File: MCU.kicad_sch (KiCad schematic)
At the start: 22 parts, among them J1 USB_C_Receptacle_USB2.0_16P, SW1 SW_Push_Open, U1 STM32H743VITx, Y1 Crystal

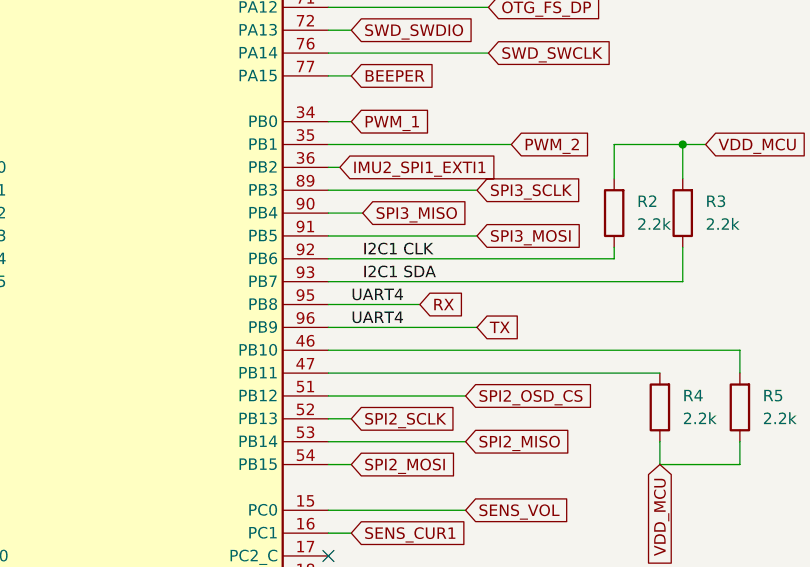
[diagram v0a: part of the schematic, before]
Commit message: finshed every schematic pages, remains footprints assignments
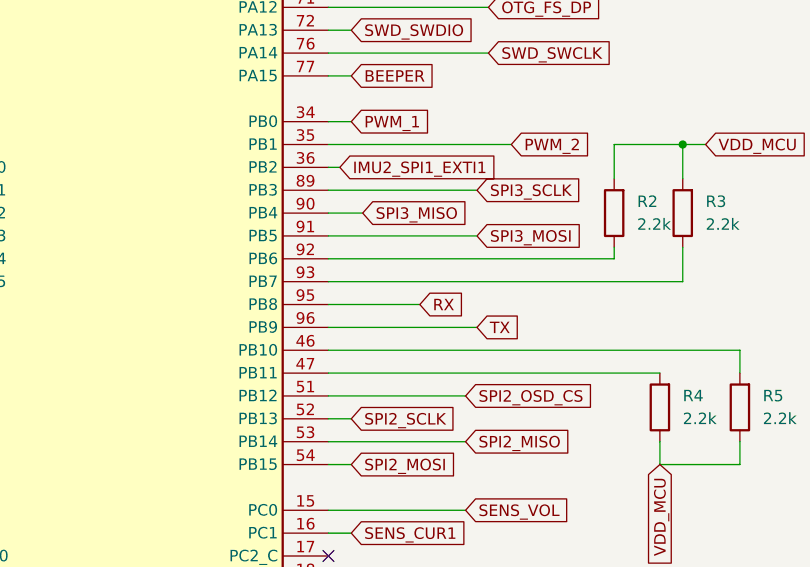
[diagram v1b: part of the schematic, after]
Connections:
- net I2C1 CLK: no longer names the net of R2.1, U1.92 (PB6)
- net I2C1 SDA: no longer names the net of R3.1, U1.93 (PB7)
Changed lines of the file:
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@@
-		)
-	)
-	(label "I2C1 CLK"
-		(at 162.56 95.25 0)
-		(effects
-			(font
-				(size 1.27 1.27)
-			)
-			(justify left bottom)
-		)
-	)
-	(label "UART4"
-		(at 161.29 102.87 0)
-		(effects
-			(font
-				(size 1.27 1.27)
-			)
-			(justify left bottom)
 		)
 	)
@@
 		(effects
 			(font
-				(size 1.27 1.27)
-			)
-			(justify left bottom)
-		)
-	)
-	(label "UART4"
-		(at 161.29 100.33 0)
-		(effects
-			(font
-				(size 1.27 1.27)
-			)
-			(justify left bottom)
-		)
-	)
-	(label "I2C1 SDA"
-		(at 162.56 97.79 0)
-		(effects
-			(font

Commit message: refactor labels U and assigned resistance footprint
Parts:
- R1, R2, R3, R4, R5, R6, R7: footprint (none) -> Resistor_SMD:R_0603_1608Metric
- Y1: Fréquence (none) -> 8M
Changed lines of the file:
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@@
 		(color 0 0 0 0)
 	)
+	(junction
+		(at 204.47 118.11)
+		(diameter 0)
+		(color 0 0 0 0)
+	)
 	(no_connect
 		(at 158.75 130.81)
@@
 	(wire
 		(pts
+			(xy 204.47 118.11) (xy 207.01 118.11)
+		)
+		(stroke
+			(width 0)
+			(type default)
+		)
+	)
+	(wire
+		(pts
 			(xy 43.18 170.18) (xy 54.61 170.18)
 		)
@@
 	(global_label "VDD_MCU"
 		(shape input)
-		(at 195.58 118.11 270)
+		(at 207.01 118.11 0)
 		(fields_autoplaced yes)
 		(effects
@@
 				(size 1.27 1.27)
 			)
-			(justify right)
+			(justify left)
 		)
 		(property "Intersheetrefs" "${INTERSHEET_REFS}"
-			(at 195.58 129.7433 90)
+			(at 218.6433 118.11 0)
 			(effects
 				(font
 					(size 1.27 1.27)
 				)
-				(justify right)
+				(justify left)
 				(hide yes)
 			)
@@
 			)
 		)
-		(property "Footprint" ""
+		(property "Footprint" "Resistor_SMD:R_0603_1608Metric"
 			(at 199.898 90.17 90)
 			(effects
@@
 			)
 		)
-		(property "Footprint" ""
+		(property "Footprint" "Resistor_SMD:R_0603_1608Metric"
 			(at 98.298 45.72 90)
 			(effects
@@
 			)
 		)
-		(property "Footprint" ""
+		(property "Footprint" "Resistor_SMD:R_0603_1608Metric"
 			(at 206.248 111.76 90)
 			(effects
@@
 			)
 		)
-		(property "Footprint" ""
+		(property "Footprint" "Resistor_SMD:R_0603_1608Metric"
 			(at 192.278 90.17 90)
 			(effects
@@
 			)
 		)
-		(property "Footprint" ""
+		(property "Footprint" "Resistor_SMD:R_0603_1608Metric"
 			(at 197.358 111.76 90)
 			(effects
@@
 			)
 		)
-		(property "Footprint" ""
+		(property "Footprint" "Resistor_SMD:R_0603_1608Metric"
 			(at 240.03 140.462 90)
 			(effects
@@
 			)
 		)
-		(property "Footprint" ""
+		(property "Footprint" "Resistor_SMD:R_0603_1608Metric"
 			(at 240.03 143.002 90)
 			(effects
@@
 		(on_board yes)
 		(dnp no)
-		(fields_autoplaced yes)
 		(property "Reference" "Y1"
 			(at 72.39 54.61 0)
@@
 			)
 		)
+		(property "Fréquence" "8M"
+			(at 68.58 59.944 0)
+			(effects
+				(font
+					(size 1.27 1.27)
+				)
+			)
+		)

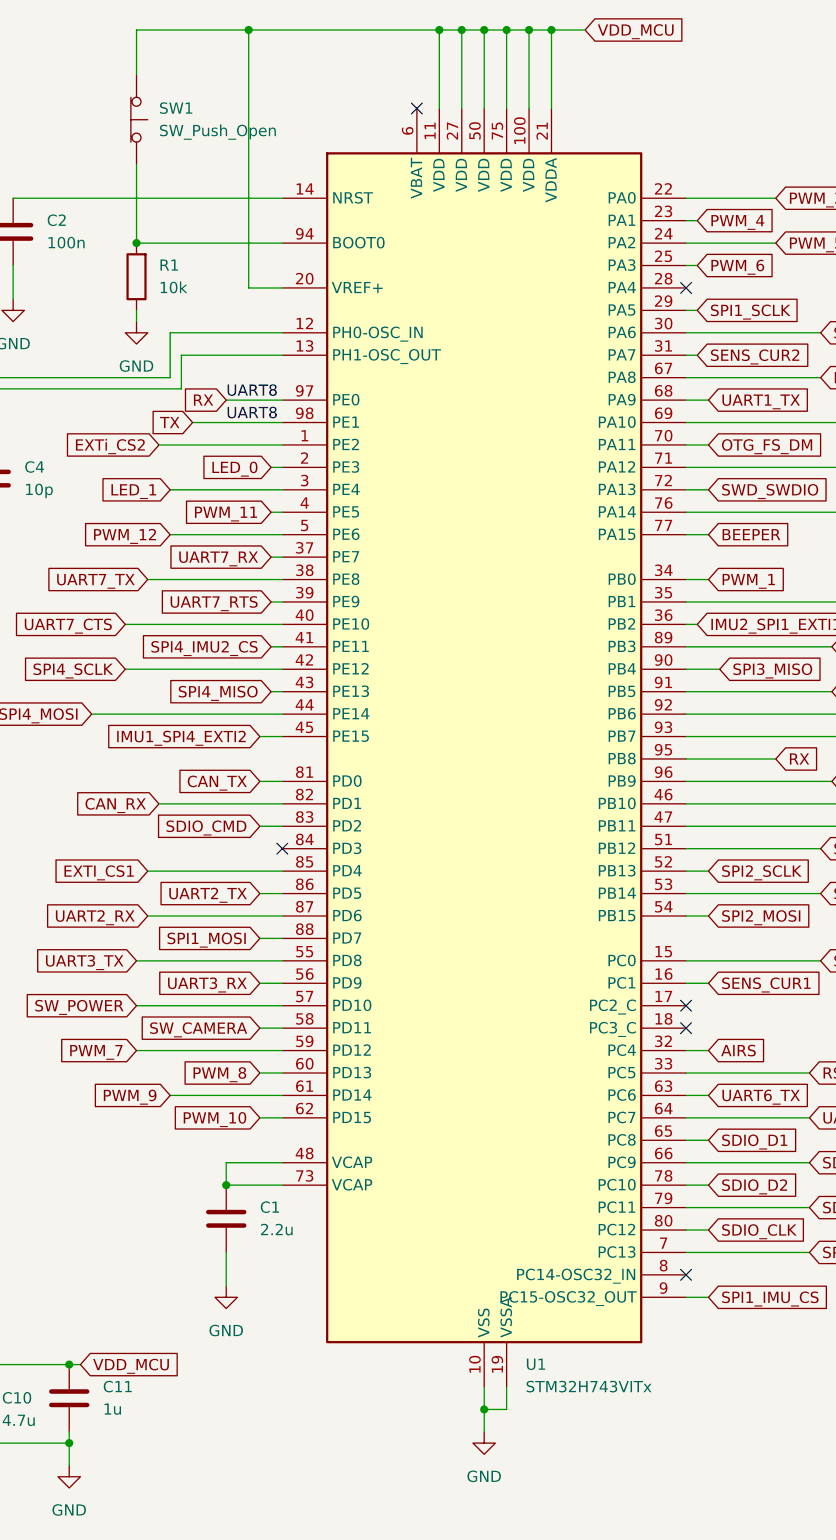
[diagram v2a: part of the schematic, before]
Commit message: refactor and update references, added some footprints
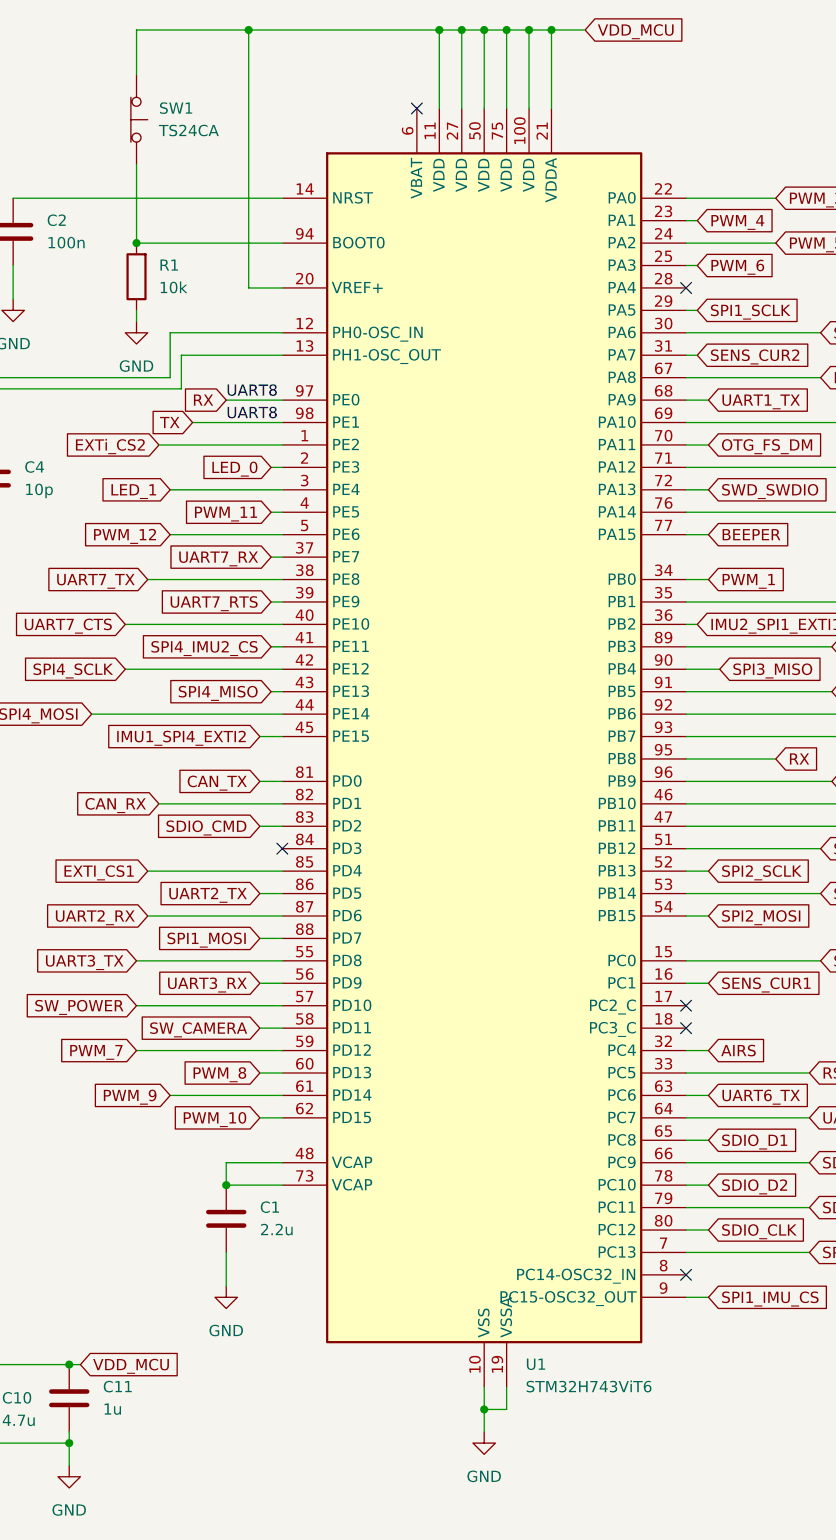
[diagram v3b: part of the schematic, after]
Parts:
- C1, C10: footprint (none) -> Capacitor_SMD:C_0805_2012Metric
- C11, C2, C3, C4, C5, C6, C7, C8, C9: footprint (none) -> Capacitor_SMD:C_0603_1608Metric
- SW1: value SW_Push_Open -> TS24CA
- U1: value STM32H743VITx -> STM32H743ViT6
- Y1: footprint (none) -> Crystal:Crystal_SMD_3225-4Pin_3.2x2.5mm
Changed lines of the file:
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@@
 			)
 		)
-		(property "Value" "STM32H743VITx"
+		(property "Value" "STM32H743ViT6"
 			(at 140.5733 171.45 0)
 			(effects
@@
 			)
 		)
-		(property "Datasheet" "https://www.st.com/resource/en/datasheet/stm32h743vi.pdf"
+		(property "Datasheet" ""
 			(at 135.89 100.33 0)
 			(effects
@@
 			)
 		)
-		(property "Value" "SW_Push_Open"
+		(property "Value" "TS24CA"
 			(at 99.06 29.2099 90)
 			(effects
@@
 			)
 		)
-		(property "Footprint" ""
+		(property "Footprint" "Capacitor_SMD:C_0603_1608Metric"
 			(at 89.8652 176.53 0)
 			(effects
@@
 			)
 		)
-		(property "Footprint" ""
+		(property "Footprint" "Capacitor_SMD:C_0603_1608Metric"
 			(at 83.5152 44.45 0)
 			(effects
@@
 			)
 		)
-		(property "Footprint" ""
+		(property "Footprint" "Capacitor_SMD:C_0805_2012Metric"
 			(at 78.4352 177.8 0)
 			(effects
@@
 			)
 		)
-		(property "Footprint" ""
+		(property "Footprint" "Capacitor_SMD:C_0603_1608Metric"
 			(at 44.1452 177.8 0)
 			(effects
@@
 			)
 		)
-		(property "Footprint" ""
+		(property "Footprint" "Capacitor_SMD:C_0603_1608Metric"
 			(at 55.5752 177.8 0)
 			(effects
@@
 			)
 		)
-		(property "Footprint" ""
+		(property "Footprint" "Capacitor_SMD:C_0603_1608Metric"
 			(at 67.0052 72.39 0)
 			(effects
@@
 			)
 		)
-		(property "Footprint" ""
+		(property "Footprint" "Capacitor_SMD:C_0603_1608Metric"
 			(at 67.0052 177.8 0)
 			(effects
@@
 			)
 		)
-		(property "Footprint" ""
+		(property "Footprint" "Capacitor_SMD:C_0603_1608Metric"
 			(at 80.9752 72.39 0)
 			(effects
@@
 			)
 		)
-		(property "Footprint" ""
+		(property "Footprint" "Crystal:Crystal_SMD_3225-4Pin_3.2x2.5mm"
 			(at 72.39 62.23 0)
 			(effects
@@
 			)
 		)
-		(property "Footprint" ""
+		(property "Footprint" "Capacitor_SMD:C_0603_1608Metric"
 			(at 21.2852 177.8 0)
 			(effects
@@
 			)
 		)
-		(property "Footprint" ""
+		(property "Footprint" "Capacitor_SMD:C_0603_1608Metric"
 			(at 32.7152 177.8 0)
 			(effects
@@
 			)
 		)
-		(property "Footprint" ""
+		(property "Footprint" "Capacitor_SMD:C_0805_2012Metric"
 			(at 107.6452 156.21 0)
 			(effects
